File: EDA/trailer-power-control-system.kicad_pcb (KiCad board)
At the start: 2 copper layers, 134.7 x 91.9 mm, 60 parts, among them IC1 AP63203WU-7, J1 Conn_01x06, J10 Conn_01x04, J11 Conn_01x04, J12 Conn_01x04, J13 Conn_01x01, J14 Conn_01x01, J2 Conn_01x04, J3 Conn_01x04, J4 Conn_01x04, J5 Conn_01x04, J6 Conn_01x04, J7 Conn_01x04, J8 Conn_01x04, J9 Conn_01x04, Q1 IRF4905STRLPBF, Q2 IRF4905STRLPBF, Q3 IRF4905STRLPBF, Q4 IRF4905STRLPBF, Q5 IRF4905STRLPBF, Q6 IRF4905STRLPBF, Q7 IRF4905STRLPBF, Q8 IRF4905STRLPBF, SW1 SW_DIP_x04, U1 ESP32-WROOM-32, U10 PC817, U11 PC817, U2 SN65HVD230, U4 PC817, U5 PC817, U6 PC817, U7 PC817, U8 PC817, U9 PC817

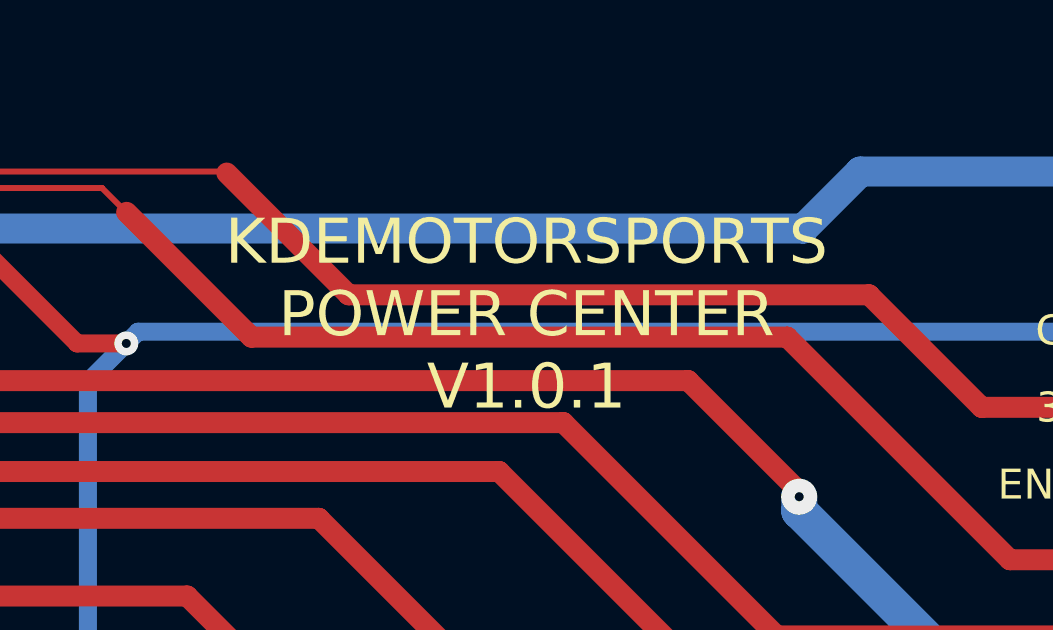
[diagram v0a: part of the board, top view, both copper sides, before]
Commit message: Logo added to case and work started to update the EDA
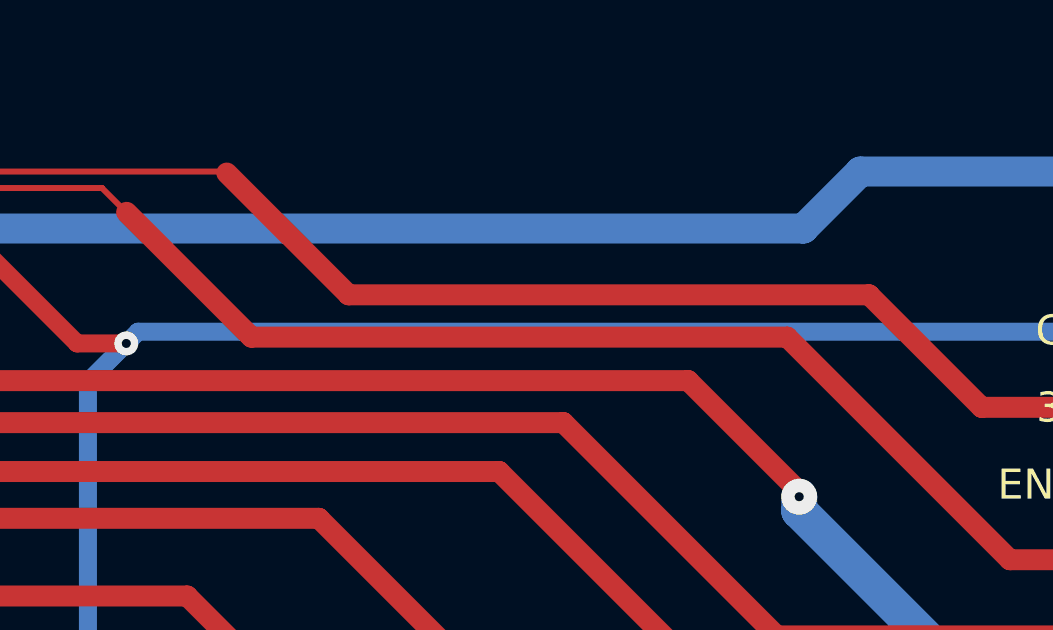
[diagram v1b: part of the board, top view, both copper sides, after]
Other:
- board text removed: "KDEMOTORSPORTS POWER CENTER V1.0.1"
